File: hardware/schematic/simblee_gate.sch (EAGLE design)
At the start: 25 parts, among them IC1 7805T, Q1 2N3906, T1 2N2222, T2 2N2222

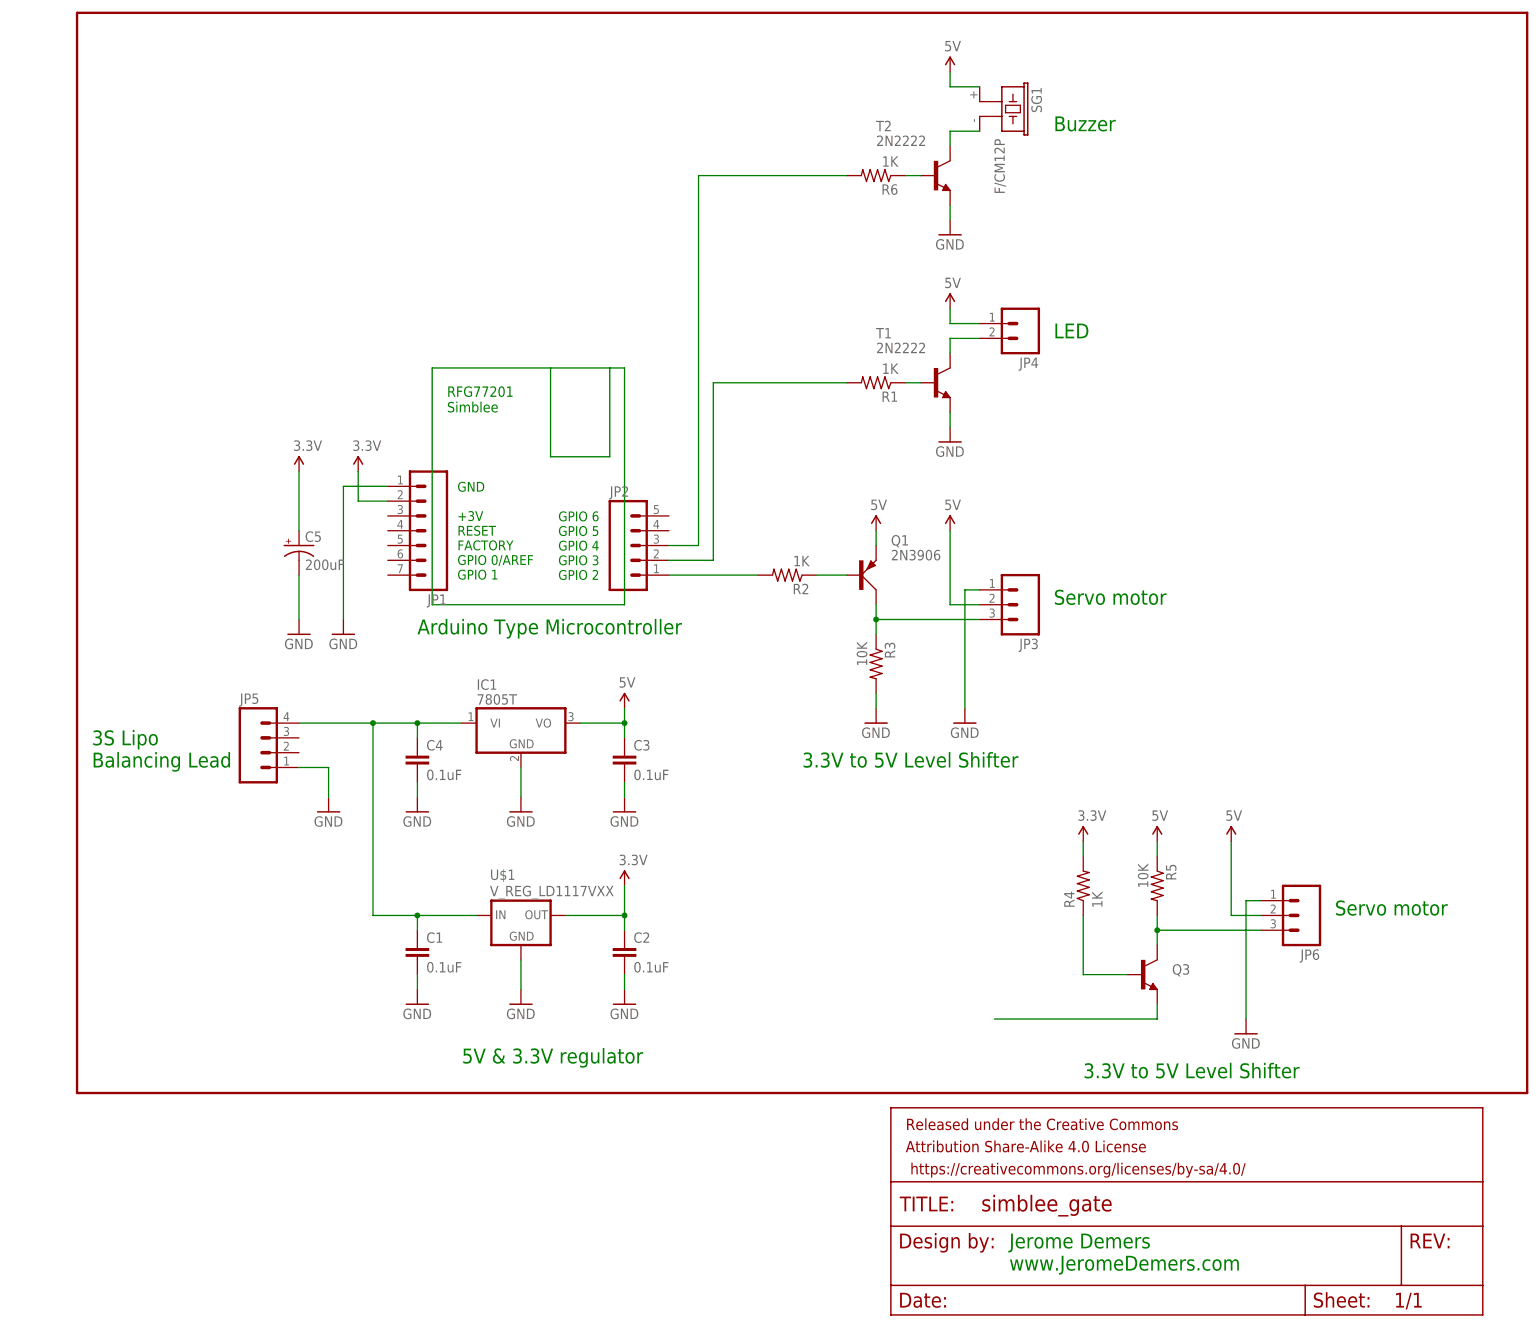
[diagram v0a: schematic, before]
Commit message: revised schematic and added PNG, BMP
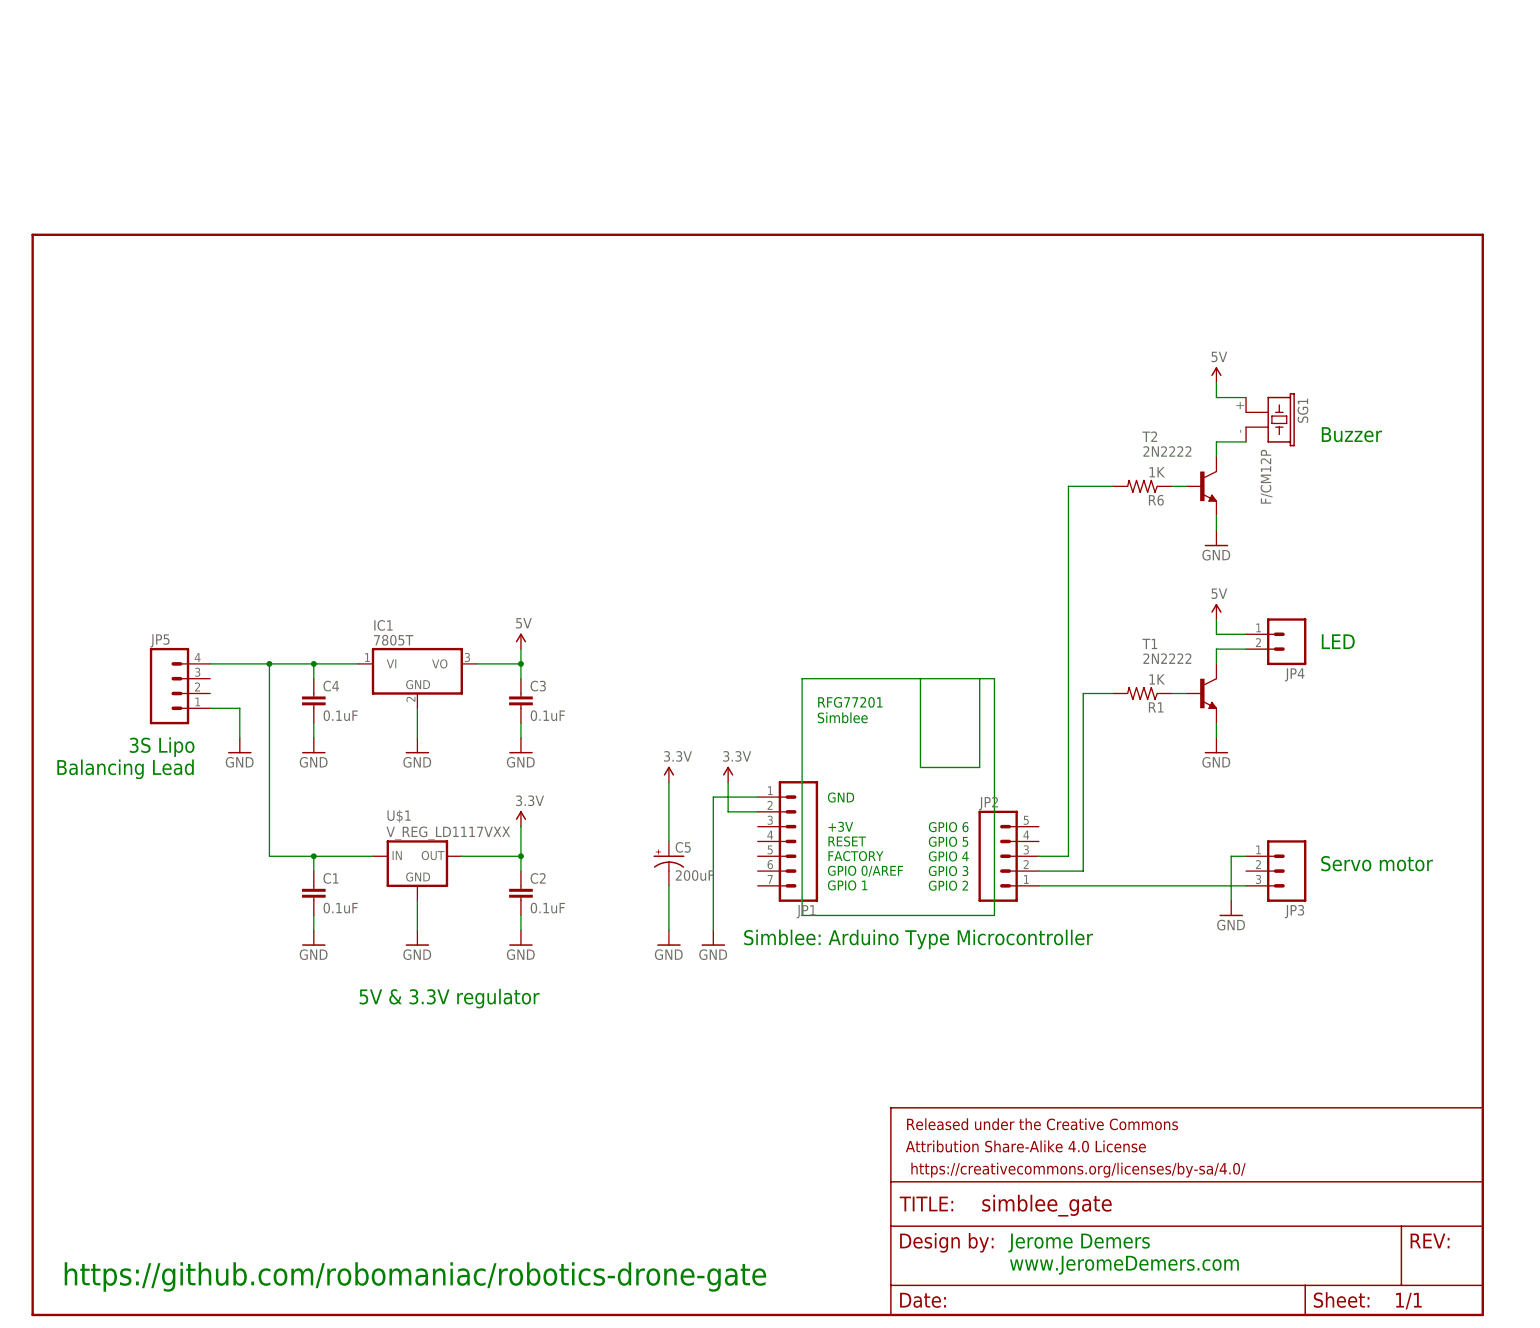
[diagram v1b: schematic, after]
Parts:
- removed JP6: (no value), SparkFun-Connectors:M03PTH
- removed Q1: 2N3906, transistor-small-signal:2N3906
- removed Q3: (no value), SparkFun-DiscreteSemi:TRANSISTOR_NPN2N3904
- removed R2, R4: 1K, SparkFun-Resistors:RESISTOR0805-RES
- removed R3, R5: 10K, SparkFun-Resistors:RESISTOR0805-RES
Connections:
- removed net N$10: JP6.3, Q3.C, R5.2
- removed net N$11: Q3.E
- removed net N$3: JP3.3, Q1.C, R3.1
- removed net N$4: JP2.1, R2.2
- removed net N$9: Q3.B, R4.1
- net GND: no longer JP6.1, R3.2
- net N$2: now also JP2.1, JP3.3; no longer Q1.B, R2.1
- net VCC: no longer JP3.2, JP6.2, Q1.E, R4.2, R5.1
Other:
- note added: "Simblee: Arduino Type Microcontroller"
- note added: "https://github.com/robomaniac/robotics-drone-gate"
- note removed: "3.3V to 5V Level Shifter"
- note removed: "Arduino Type Microcontroller"
- moved on the sheet: C1, C2, C3, C4, C5, IC1, JP1, JP2, JP3, JP4, JP5, R1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
